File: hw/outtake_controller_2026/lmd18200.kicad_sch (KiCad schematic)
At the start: 2 parts, among them U2 LMD18200T_NOPB

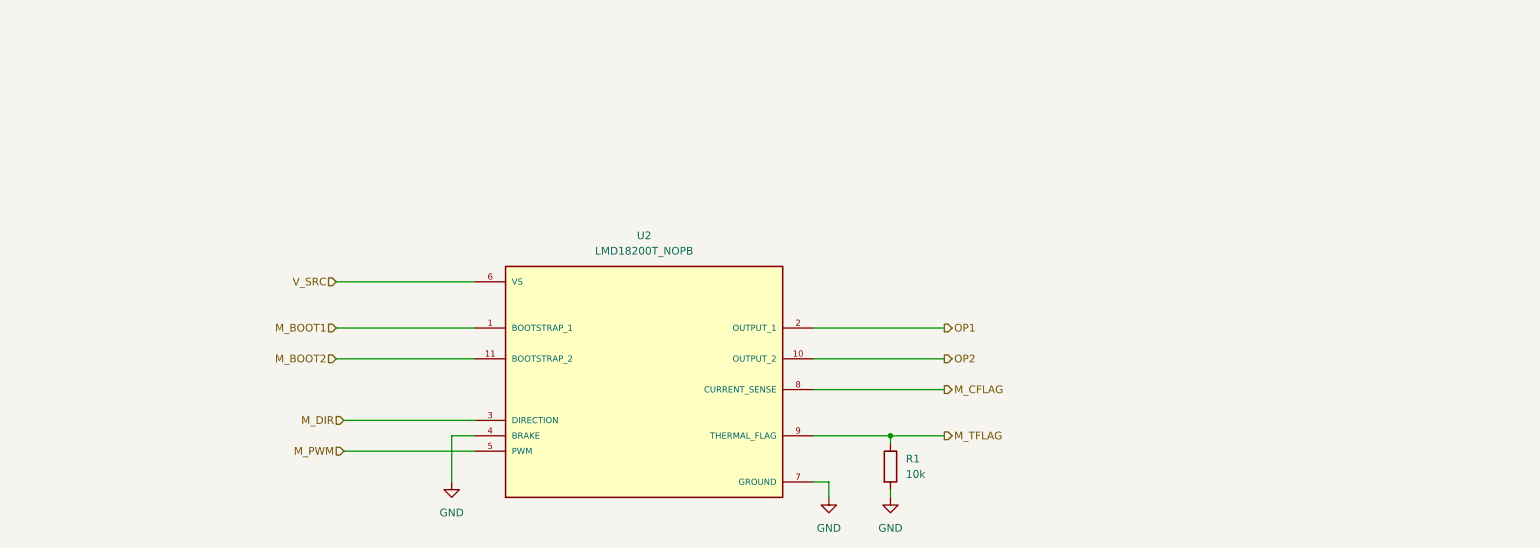
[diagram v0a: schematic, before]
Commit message: finished actuator board, includes zip folder of project and gerbers used to order board
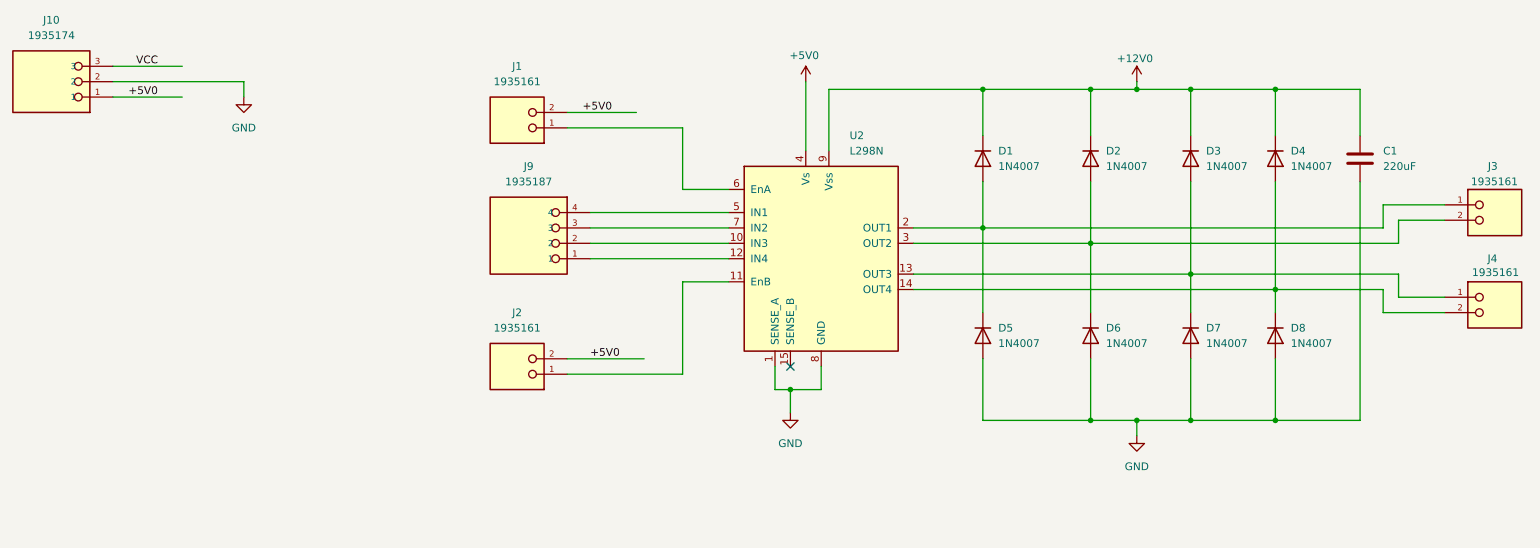
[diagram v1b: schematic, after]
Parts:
- removed R1: 10k, symbol Device:R
- removed U2: LMD18200T_NOPB, LMD18200T_NOPB:TO170P2027X462X2082-11, symbol outtake_controller_2026_parts_library:LMD18200T_NOPB
- added C1: 220uF, symbol Device:C
- added D1, D2, D3, D4, D5, D6, D7, D8: 1N4007, Diode_THT:D_DO-41_SOD81_P10.16mm_Horizontal, symbol Diode:1N4007
- added J1, J2, J3, J4: 1935161, 1935161:PHOENIX_1935161, symbol outtake_controller_2026_parts_library:1935161
- added J10: 1935174, 1935174:PHOENIX_1935174, symbol outtake_controller_2026_parts_library:1935174
- added J9: 1935187, 1935187:PHOENIX_1935187, symbol outtake_controller_2026_parts_library:1935187
- added U2: L298N, Package_TO_SOT_THT:TO-220-15_P2.54x2.54mm_StaggerOdd_Lead4.58mm_Vertical, symbol Driver_Motor:L298N
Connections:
- net GND: now also C1.2, D5.2 (A), D6.2 (A), D7.2 (A), D8.2 (A), J10.2, U2.1 (SENSE_A), U2.8 (GND)
- new net: D4.2 (A), D8.1 (K), J4.2, U2.14 (OUT4)
- new net: J2.1, U2.11 (EnB)
- new net: J9.2, U2.10 (IN3)
- new net: J9.1, U2.12 (IN4)
- new net: D3.2 (A), D7.1 (K), J4.1, U2.13 (OUT3)
- new net: D1.2 (A), D5.1 (K), J3.1, U2.2 (OUT1)
- new net: D2.2 (A), D6.1 (K), J3.2, U2.3 (OUT2)
- new net: J9.4, U2.5 (IN1)
- new net: J1.1, U2.6 (EnA)
- new net: J9.3, U2.7 (IN2)
- new net +12V0: C1.1, D1.1 (K), D2.1 (K), D3.1 (K), D4.1 (K), U2.9 (Vss)
- new net +5V0: J1.2, J10.1, J2.2, U2.4 (Vs)
- new net VCC: J10.3
- no-connect marks 0 -> 1
